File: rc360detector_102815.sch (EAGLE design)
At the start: 14 parts, among them IC2 LM317MSTT3, X1 SSW-101-02-S-D, X4 87758-0616, X5 87758-0616, X6 87758-0616

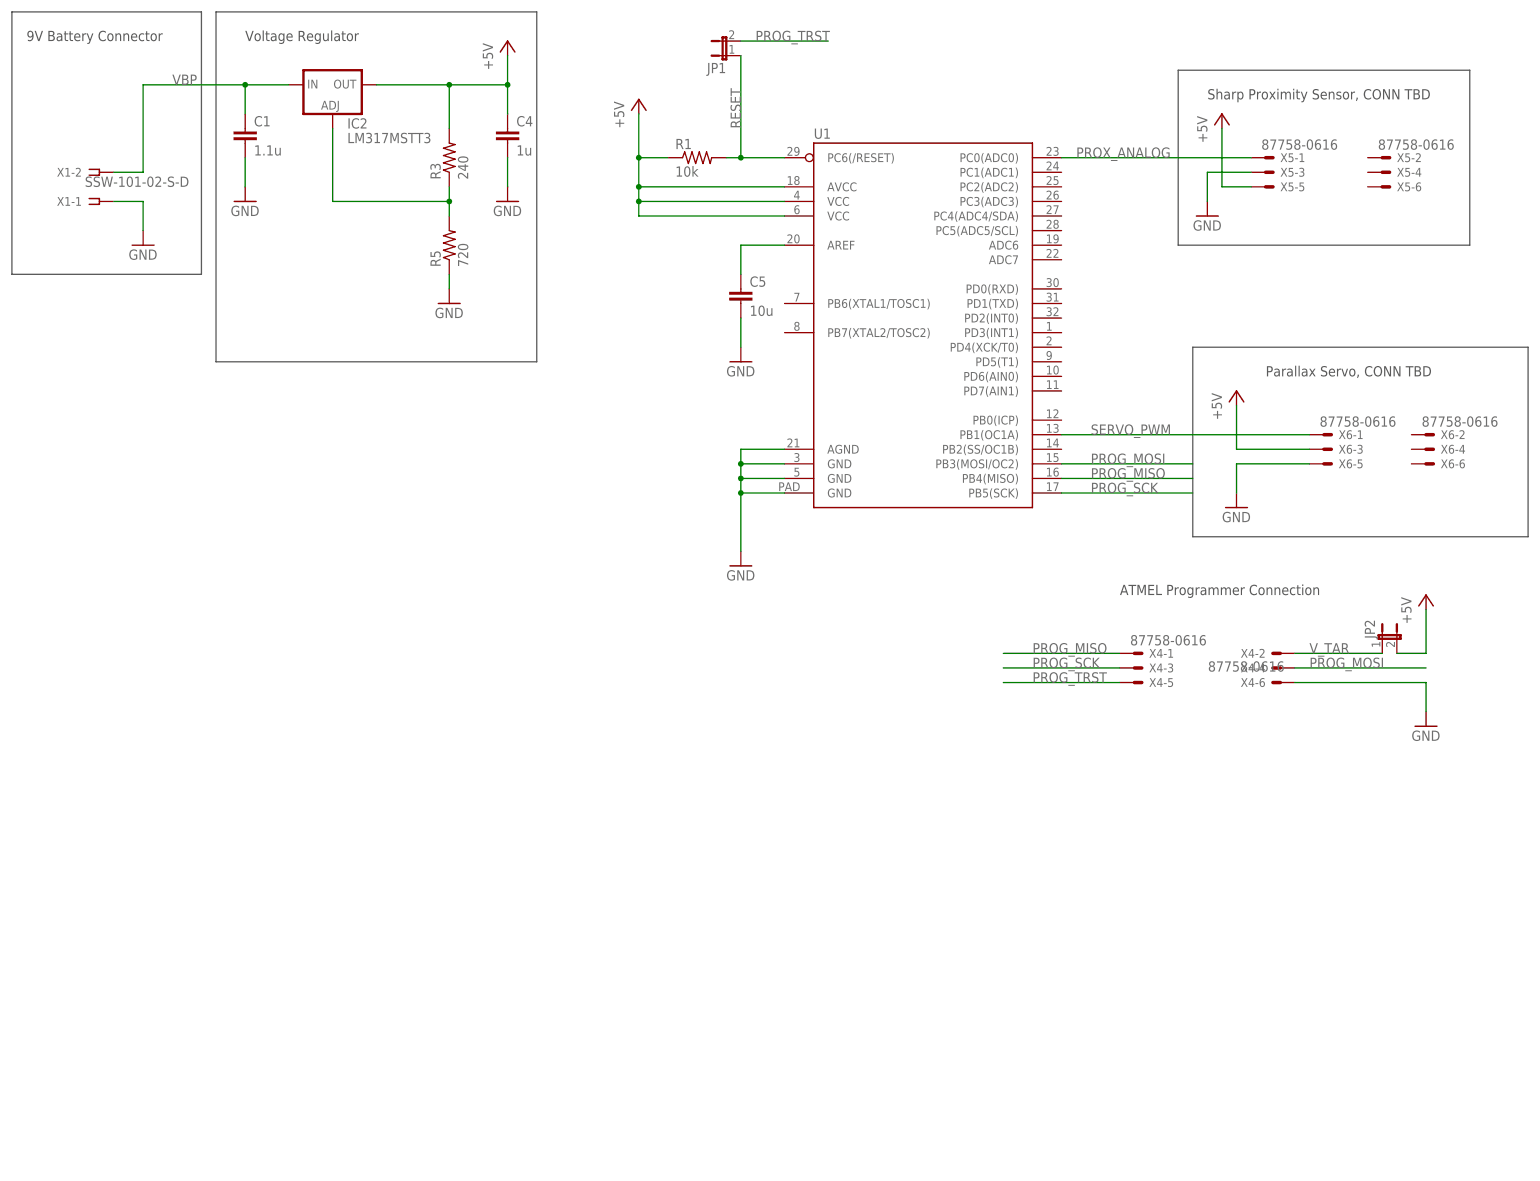
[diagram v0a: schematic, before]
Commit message: Update
-Added RGB LEDs
-Reorganized layout
-Added TWI (aka I2C) interface connections
-Added Test points to critical signals
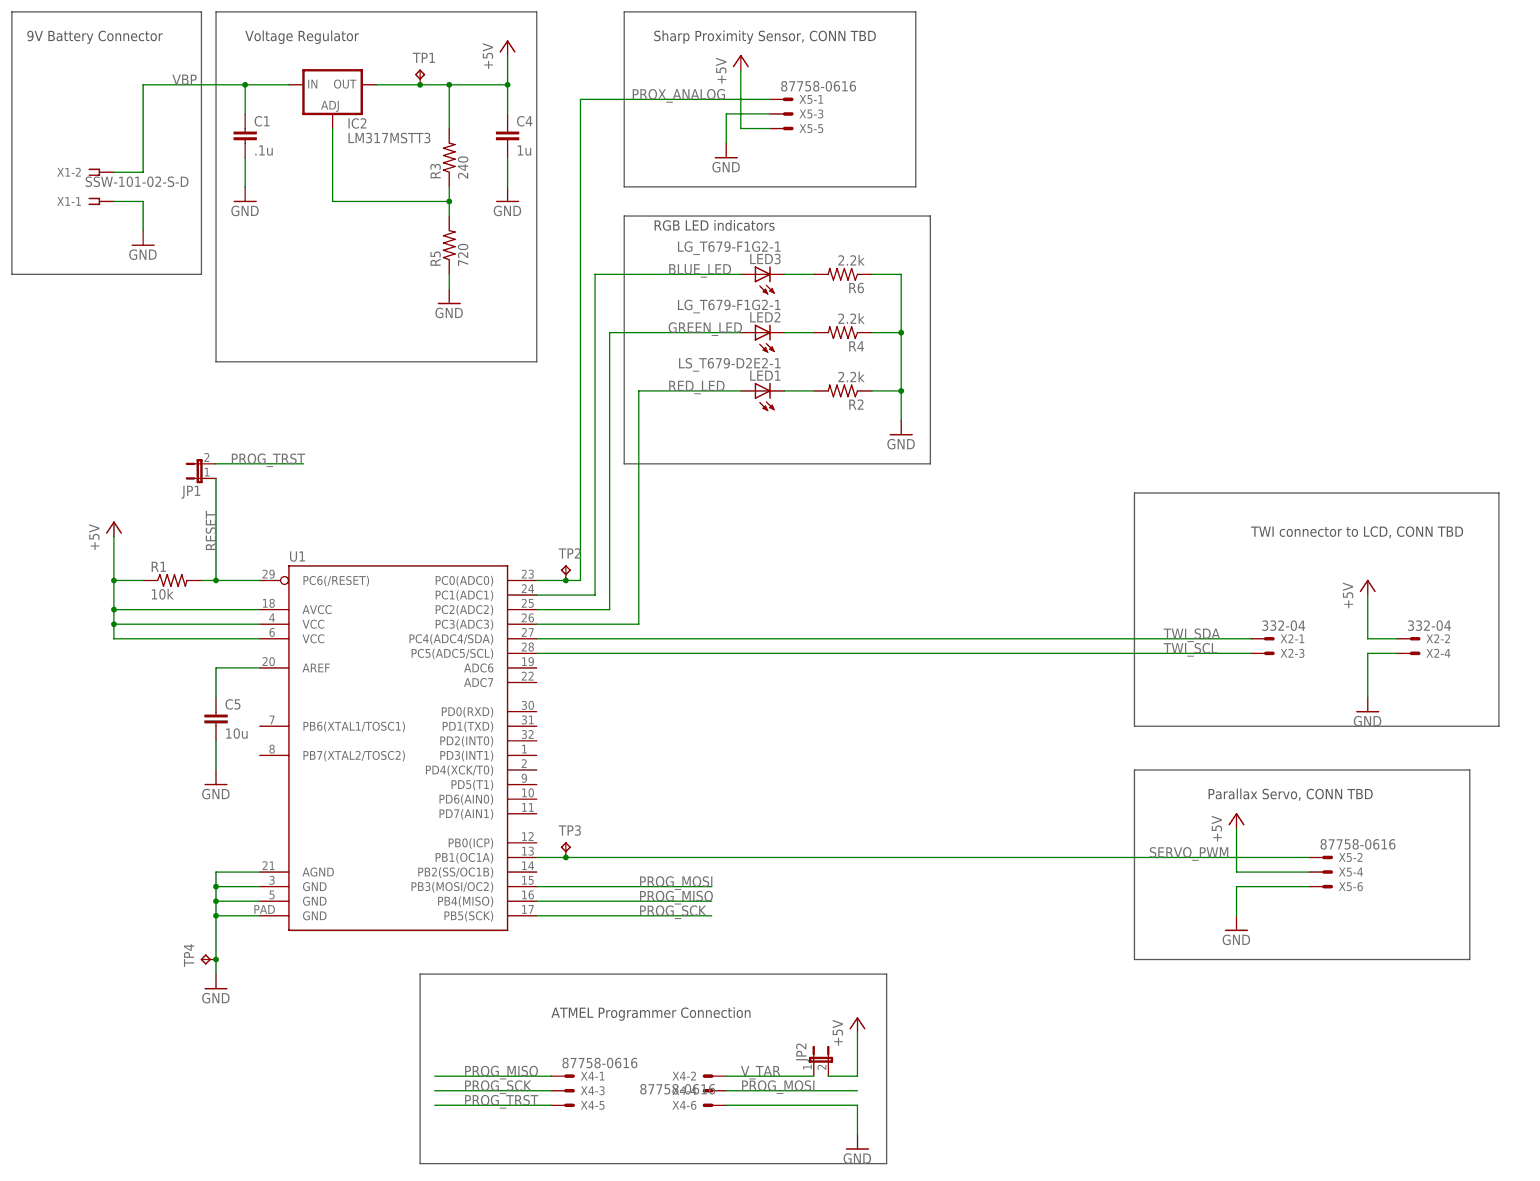
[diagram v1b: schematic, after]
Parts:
- removed X6: 87758-0616, con-molex:87758-0616
- added LED1: LS_T679-D2E2-1, led:LS_T679-D2E2-1
- added LED2, LED3: LG_T679-F1G2-1, led:LG_T679-F1G2-1
- added R2, R4, R6: 2.2k, rcl:R-US_R0805
- added TP1, TP2, TP3, TP4: TPPAD1-17, testpad:TPPAD1-17
- added X2: 332-04, con-garry:332-04
- C1: value 1.1u -> .1u
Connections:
- new net BLUE_LED: LED3.A, U1.PC1(ADC1)
- new net GREEN_LED: LED2.A, U1.PC2(ADC2)
- new net N$5: LED3.C, R6.2
- new net N$7: LED2.C, R4.2
- new net N$8: LED1.C, R2.2
- new net RED_LED: LED1.A, U1.PC3(ADC3)
- new net TWI_SCL: U1.PC5(ADC5/SCL), X2-3.S
- new net TWI_SDA: U1.PC4(ADC4/SDA), X2-1.S
- net +5V: now also TP1.TP, X2-2.S, X5-4.S; no longer X6-3.S
- net GND: now also R2.1, R4.1, R6.1, TP4.TP, X2-4.S, X5-6.S; no longer X6-5.S
- net PROX_ANALOG: now also TP2.TP
- net SERVO_PWM: now also TP3.TP, X5-2.S; no longer X6-1.S
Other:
- note added: "RGB LED indicators"
- note added: "TWI connector to LCD, CONN TBD"
- moved on the sheet: C5, JP1, JP2, R1, U1, X4-1, X4-2, X4-3, X4-4, X4-5, X4-6, X5-1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
